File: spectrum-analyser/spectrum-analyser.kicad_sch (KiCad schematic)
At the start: 26 parts, among them J1 Conn_Coaxial, Q1 PMOS, Q2 PMOS, Q3 Q_PMOS_GSD, SW1 SW_SPDT, SW2 SW_UP, SW3 SW_RIGHT, SW4 SW_LEFT, SW5 SW_DOWN, U1 1.3" OLED, U2 ESP32-C3_Zero, U3 LM1117MP-3.3, U4 RX5808(V3.3)

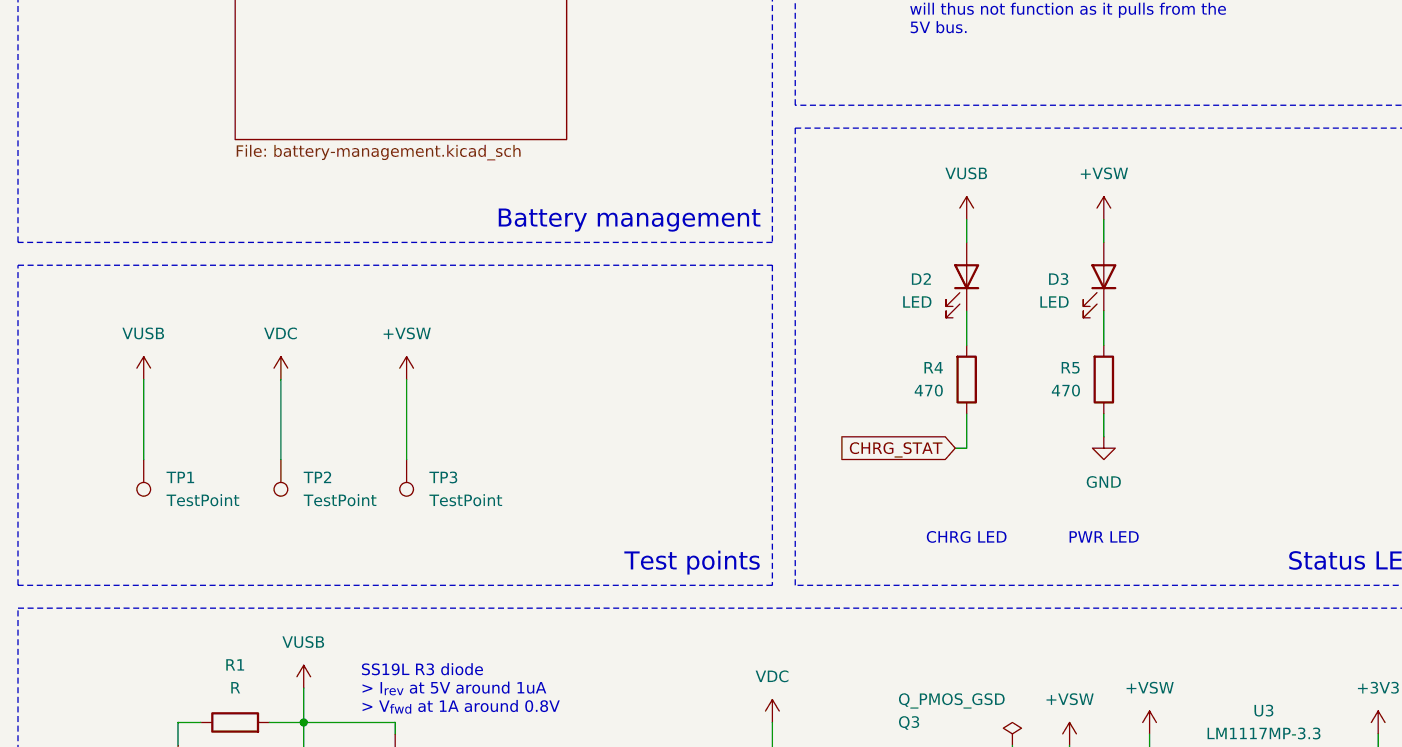
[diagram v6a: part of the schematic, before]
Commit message: Add mounting holes
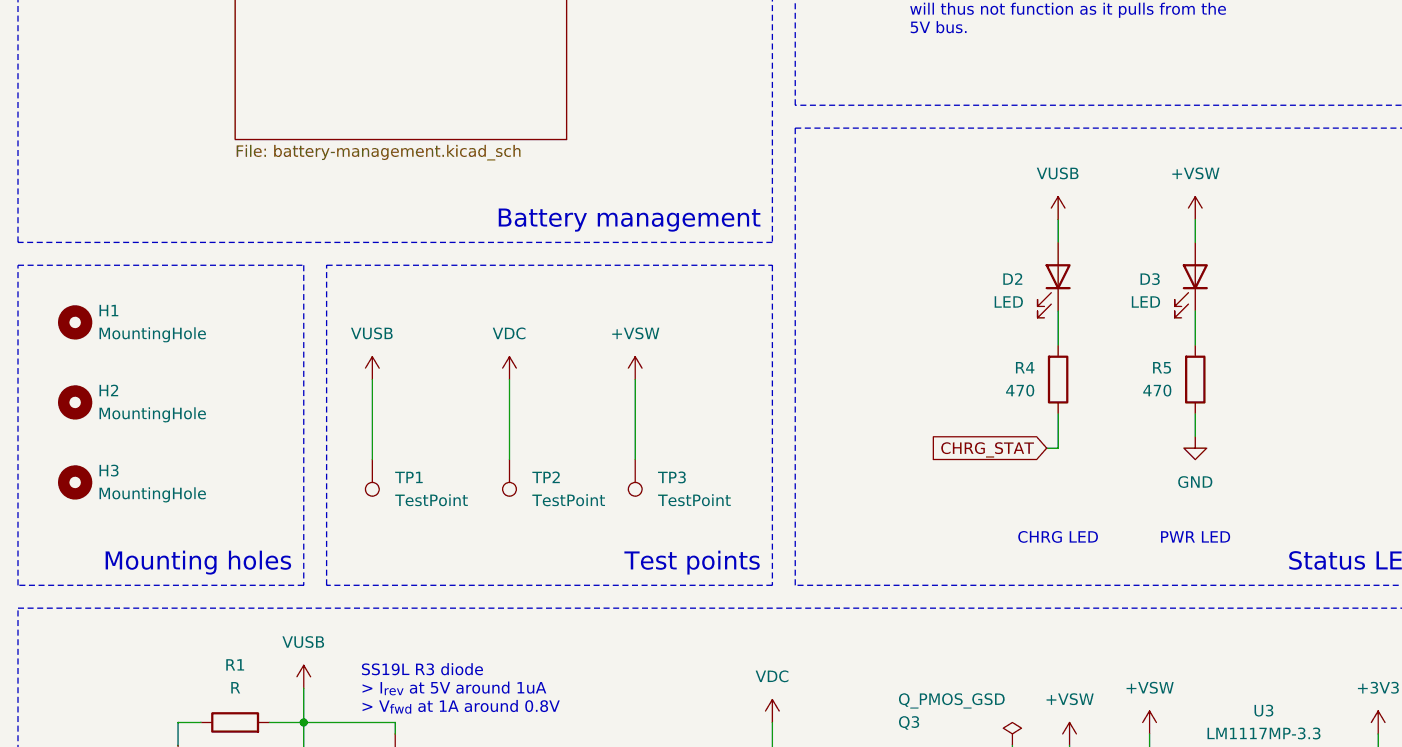
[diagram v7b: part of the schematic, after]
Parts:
- added H1, H2, H3: MountingHole, MountingHole:MountingHole_2.7mm_M2.5, symbol Mechanical:MountingHole
- TP1, TP2, TP3: footprint TestPoint:TestPoint_Pad_D3.0mm -> TestPoint:TestPoint_Pad_D2.0mm
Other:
- note added: "Mounting holes"
- moved on the sheet: D2, D3, R4, R5, TP1, TP2, TP3

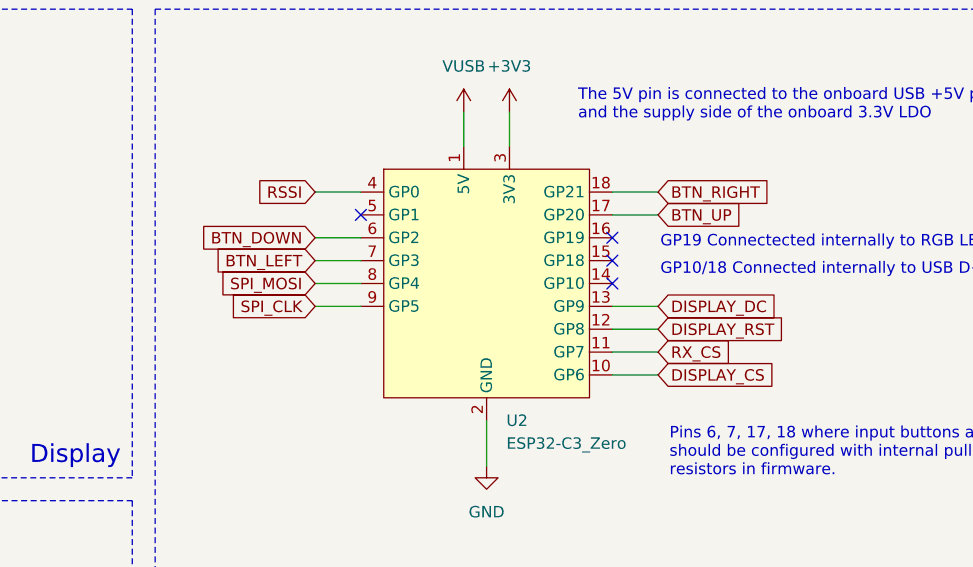
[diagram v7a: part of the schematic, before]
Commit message: Route signal traces and adjust mcu module pin assignment
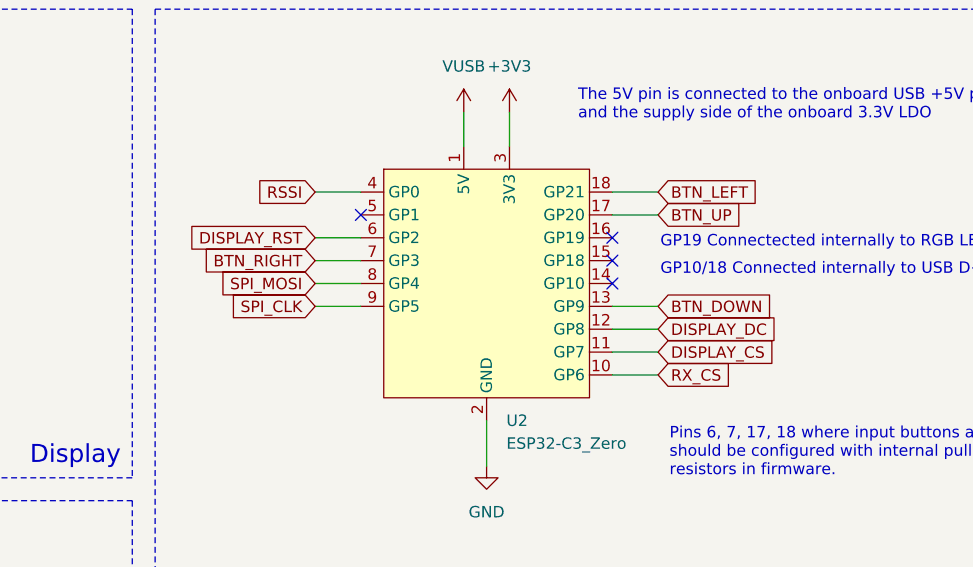
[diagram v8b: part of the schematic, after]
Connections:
- net BTN_DOWN: now also U2.13 (GP9); no longer U2.6 (GP2)
- net BTN_LEFT: now also U2.18 (GP21); no longer U2.7 (GP3)
- net BTN_RIGHT: now also U2.7 (GP3); no longer U2.18 (GP21)
- net DISPLAY_CS: now also U2.11 (GP7); no longer U2.10 (GP6)
- net DISPLAY_DC: now also U2.12 (GP8); no longer U2.13 (GP9)
- net DISPLAY_RST: now also U2.6 (GP2); no longer U2.12 (GP8)
- net RX_CS: now also U2.10 (GP6); no longer U2.11 (GP7)
